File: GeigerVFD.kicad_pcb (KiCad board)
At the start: 2 copper layers, 137.2 x 114.3 mm, 68 parts, among them IC1 TLC555, IC2 LM555, J1 5V, J2 3.3V, J3 GND, J4 Pulse, Q1 BD137, T1 STN0214, T2 2N4401, T3 2N4401, T4 Transformer_1P_SS, U1 LM2577, U2 ESP32-DEVKITC-32D, U3 MAX6934, U4 FV651G

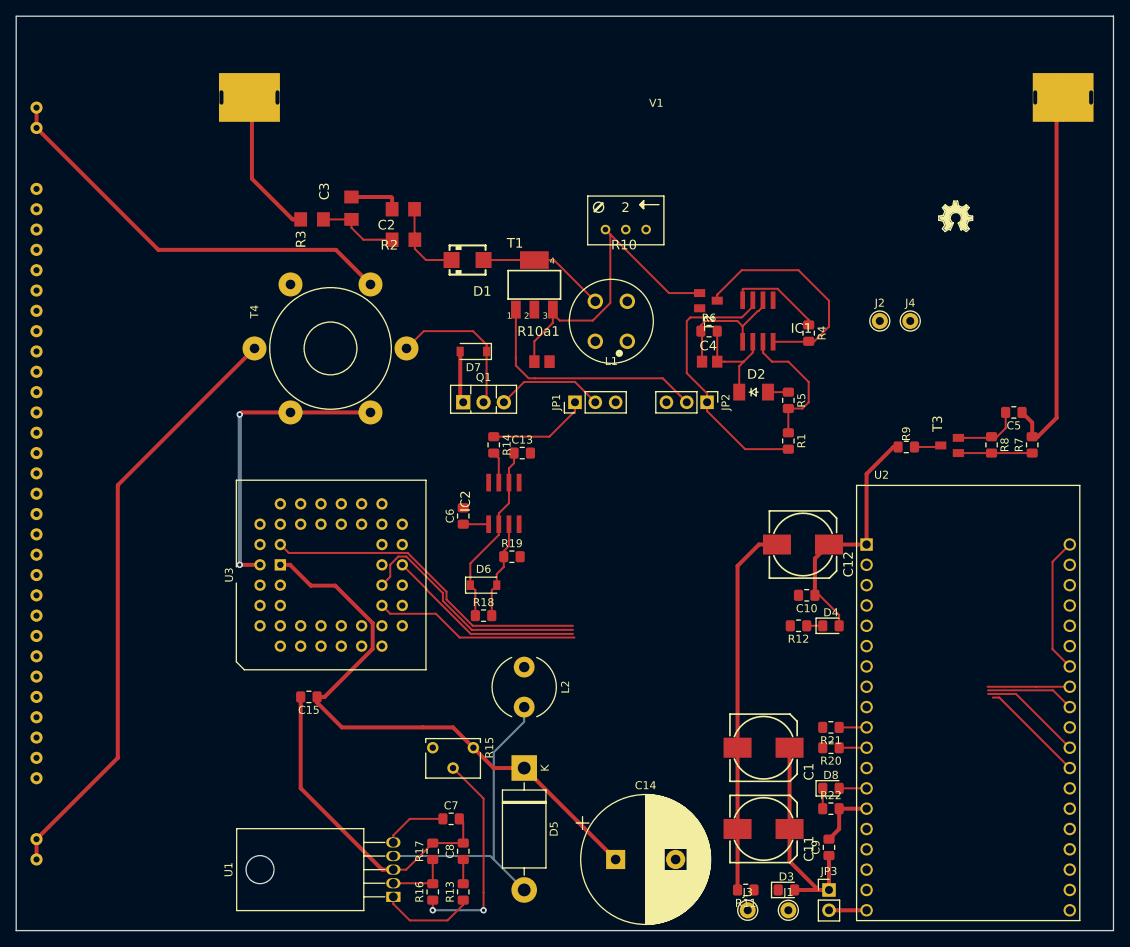
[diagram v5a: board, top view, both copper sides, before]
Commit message: Shrink & route & add rotary encoder & add 3d models
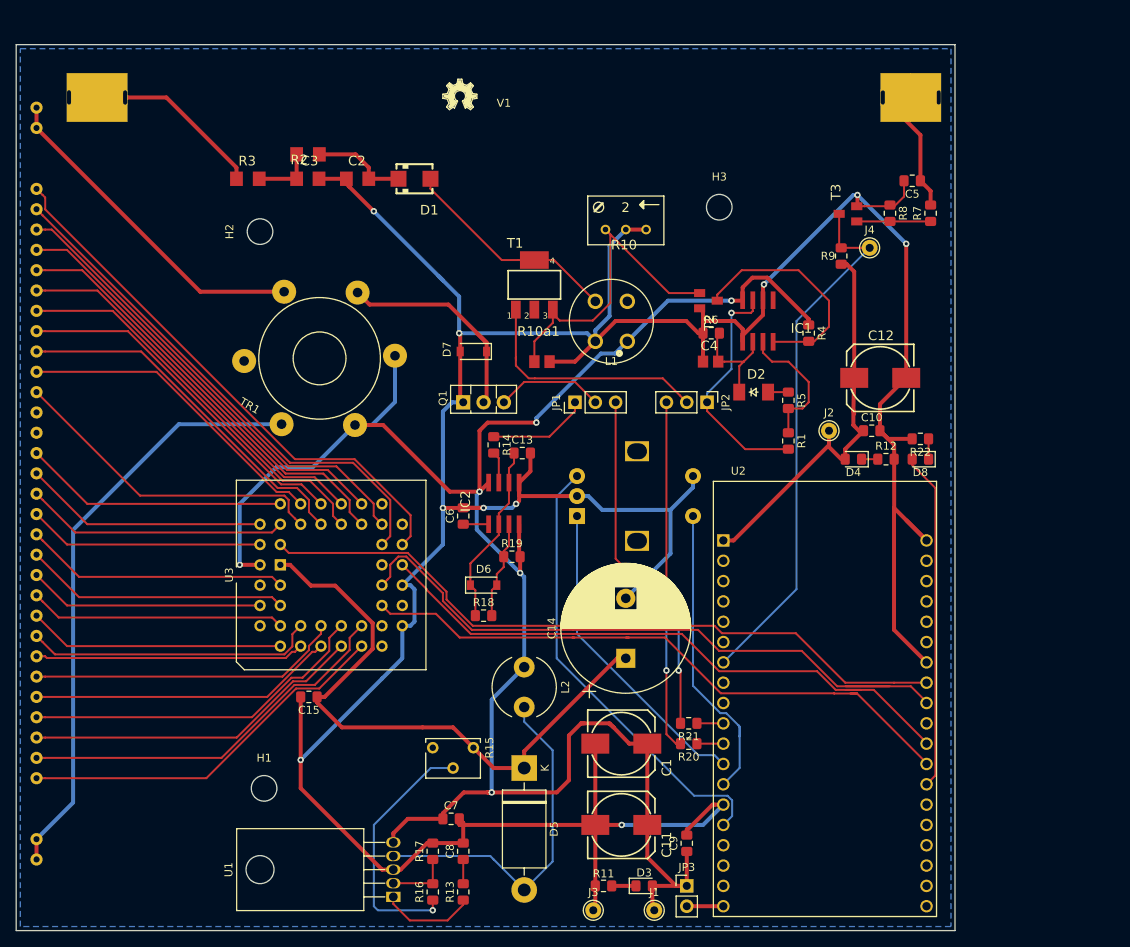
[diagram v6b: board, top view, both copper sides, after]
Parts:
- added H1: MountingHole, MountingHole:MountingHole_3.2mm_M3_DIN965, F.Cu at (29.5, 302.8)
- added H2: MountingHole, MountingHole:MountingHole_3.2mm_M3_DIN965, F.Cu at (29.0, 233.2)
- added H3: MountingHole, MountingHole:MountingHole_3.2mm_M3_DIN965, F.Cu at (86.4, 230.1)
- added SW1: Rotary_Encoder_Switch, Rotary_Encoder:RotaryEncoder_Alps_EC12E-Switch_Vertical_H20mm, B.Cu at (68.6, 268.7)
- moved LOGO1 63.8 mm to (51.8, 217.9)
- moved R22 47.6 mm to (111.5, 259.1), turned to 180 degrees
- moved D8 42.6 mm to (111.5, 261.6), turned to 180 degrees
- moved R7 31.6 mm to (112.8, 230.9)
- moved R8 31.6 mm to (107.7, 230.9)
- moved T3 31.6 mm to (102.4, 231.0)
- moved C5 31.6 mm to (110.5, 226.8)
- moved R9 25.2 mm to (101.6, 236.2), turned to 90 degrees
- moved C14 25.2 mm to (74.7, 286.5), turned to 90 degrees
- moved R12 23.5 mm to (107.2, 261.6), turned to 0 degrees
- moved C12 23.0 mm to (106.5, 251.5), turned to 180 degrees
- moved C10 22.1 mm to (105.4, 258.1), turned to 0 degrees
- moved D4 21.0 mm to (103.1, 261.6), turned to 180 degrees
- moved J3 19.3 mm to (70.6, 318.0)
- moved V1 19.1 mm to (59.4, 216.4)
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- renumbered T4 to TR1
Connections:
- net Net-(U3-Pad34) renamed /05G
- U2 pad 12: (no net) -> Net-(SW1-PadA)
- U2 pad 13: Net-(D8-Pad2) -> Net-(SW1-PadS1)
- U2 pad 15: (no net) -> Net-(SW1-PadB)
- U2 pad 32: (no net) -> Net-(D8-Pad2)
- U3 pad 10: Net-(U3-Pad10) -> /P10
- U3 pad 11: Net-(U3-Pad11) -> /P13
- U3 pad 12: Net-(U3-Pad12) -> /P12
- U3 pad 13: Net-(U3-Pad13) -> /P15
- U3 pad 14: Net-(U3-Pad14) -> /P14
- U3 pad 15: Net-(U3-Pad15) -> /P17
- U3 pad 16: Net-(U3-Pad16) -> /P16
- U3 pad 17: Net-(U3-Pad17) -> (no net)
- U3 pad 19: Net-(U3-Pad19) -> (no net)
- U3 pad 20: Net-(U3-Pad20) -> (no net)
- U3 pad 25: Net-(U3-Pad25) -> (no net)
- U3 pad 26: (no net) -> /11G
- U3 pad 27: (no net) -> /10G
- U3 pad 3: Net-(U3-Pad3) -> /P05
- U3 pad 30: Net-(U3-Pad30) -> /09G
- U3 pad 31: Net-(U3-Pad31) -> /08G
- U3 pad 32: Net-(U3-Pad32) -> /07G
- U3 pad 33: Net-(U3-Pad33) -> /06G
- U3 pad 35: Net-(U3-Pad35) -> /04G
- U3 pad 36: Net-(U3-Pad36) -> /03G
- U3 pad 37: Net-(U3-Pad37) -> /02G
- U3 pad 38: Net-(U3-Pad38) -> /01G
- U3 pad 39: Net-(U3-Pad39) -> /P01
- U3 pad 4: Net-(U3-Pad4) -> /P07
- U3 pad 40: Net-(U3-Pad40) -> /P02
- U3 pad 41: (no net) -> /P03
- U3 pad 42: (no net) -> /P04
- U3 pad 5: Net-(U3-Pad5) -> /P06
- U3 pad 7: Net-(U3-Pad7) -> /P09
- U3 pad 8: Net-(U3-Pad8) -> /P08
- U3 pad 9: Net-(U3-Pad9) -> /P11
- U4 pad 10: Net-(U3-Pad9) -> /P12
- U4 pad 11: Net-(U3-Pad10) -> /P11
- U4 pad 12: Net-(U3-Pad11) -> /P10
- U4 pad 13: Net-(U3-Pad12) -> /P09
- U4 pad 14: Net-(U3-Pad13) -> /P08
- U4 pad 15: Net-(U3-Pad14) -> /P07
- U4 pad 16: Net-(U3-Pad15) -> /P06
- U4 pad 17: Net-(U3-Pad16) -> /P05
- U4 pad 18: Net-(U3-Pad17) -> /P04
- U4 pad 19: Net-(U3-Pad19) -> /P03
- U4 pad 20: Net-(U3-Pad20) -> /P02
- U4 pad 21: Net-(U3-Pad25) -> /P01
- U4 pad 24: Net-(U3-Pad30) -> /01G
- U4 pad 25: Net-(U3-Pad31) -> /02G
- U4 pad 26: Net-(U3-Pad32) -> /03G
- U4 pad 27: Net-(U3-Pad33) -> /04G
- U4 pad 29: Net-(U3-Pad35) -> /06G
- U4 pad 30: Net-(U3-Pad36) -> /07G
- U4 pad 31: Net-(U3-Pad37) -> /08G
- U4 pad 32: Net-(U3-Pad38) -> /09G
- U4 pad 33: Net-(U3-Pad39) -> /10G
- U4 pad 34: Net-(U3-Pad40) -> /11G
- U4 pad 5: Net-(U3-Pad3) -> /P17
- U4 pad 6: Net-(U3-Pad4) -> /P16
- U4 pad 7: Net-(U3-Pad5) -> /P15
- U4 pad 8: Net-(U3-Pad7) -> /P14
- U4 pad 9: Net-(U3-Pad8) -> /P13
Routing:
- net GND: track 150.1 -> 444.8 mm, vias 0 -> 10
- net +5V: track 86.8 -> 247.4 mm, vias 2 -> 6
- net /11G: track 0.00 -> 68.6 mm
- net /10G: track 0.00 -> 65.3 mm
- net Net-(J4-Pad1): track 3.36 -> 67.3 mm
- net /09G: track 0.00 -> 59.3 mm
- net Net-(SW1-PadB): track 0.00 -> 56.6 mm
- net /07G: track 0.00 -> 54.7 mm
- net /08G: track 0.00 -> 53.8 mm
- net /05G: track 0.00 -> 50.0 mm
- net /06G: track 0.00 -> 49.1 mm
- net /P16: track 0.00 -> 48.4 mm
- net /P17: track 0.00 -> 47.5 mm
- net Net-(JP1-Pad3): track 0.00 -> 47.3 mm, vias 0 -> 2
- net /03G: track 0.00 -> 45.4 mm
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- added copper zone on B.Cu, net GND
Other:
- board size 137.2 x 114.3 mm -> 117.3 x 110.7 mm

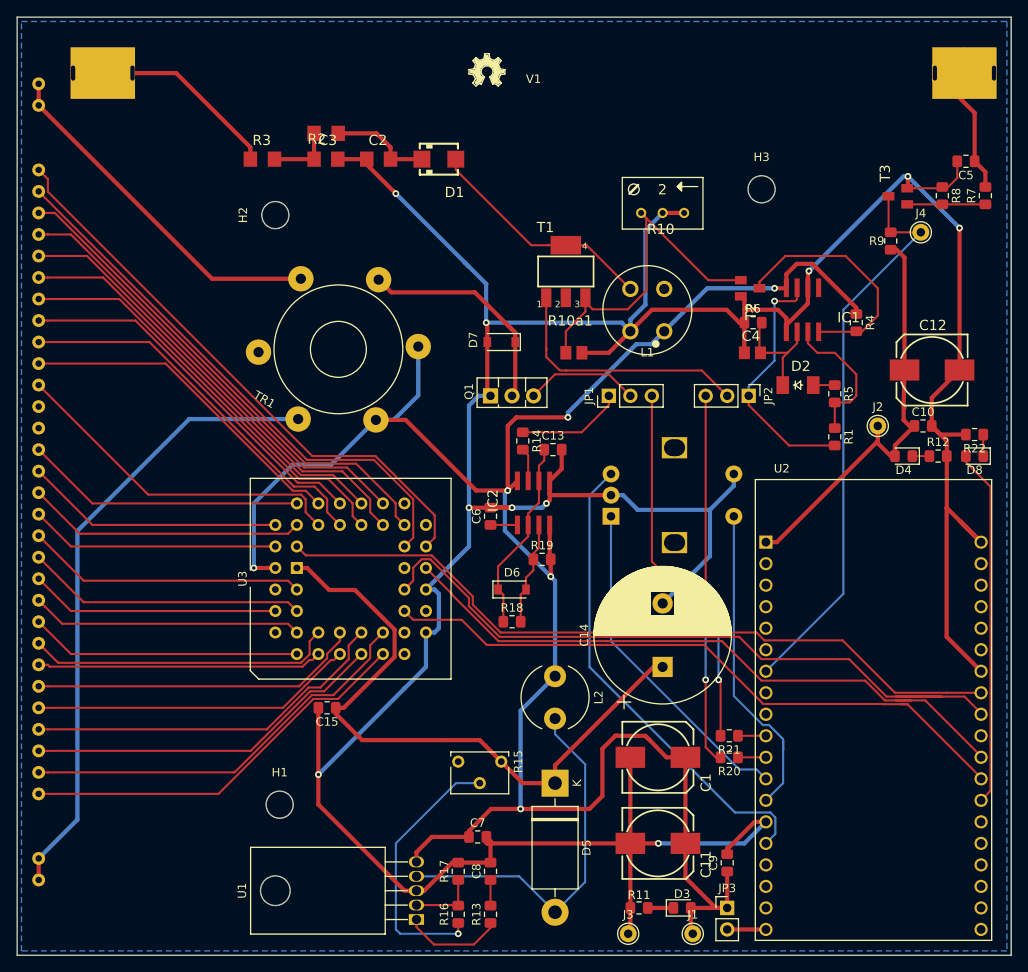
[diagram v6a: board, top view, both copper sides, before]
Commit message: Convert Eagle R to Kicad Add Buzzer header & Warn LED
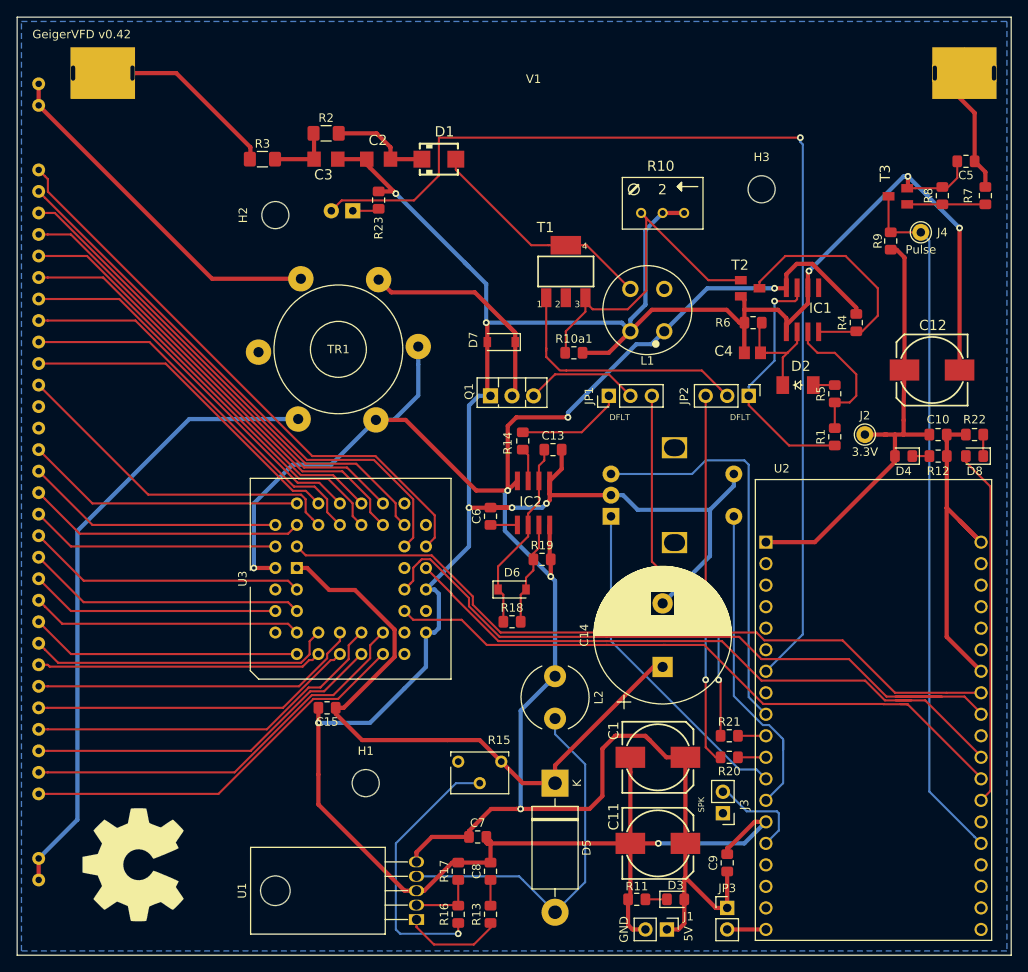
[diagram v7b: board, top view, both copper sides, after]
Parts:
- added D9: red, LED_THT:LED_D5.0mm, B.Cu at (38.1, 232.7)
- added R23: 1k, Resistor_SMD:R_0805_2012Metric_Pad1.15x1.40mm_HandSolder, F.Cu at (41.1, 231.4)
- J1: value 5V -> Conn_01x02_Male; footprint Connector_Pin:Pin_D1.0mm_L10.0mm -> Connector_PinHeader_2.54mm:PinHeader_1x02_P2.54mm_Vertical
- J3: value GND -> Conn_01x02_Male; footprint Connector_Pin:Pin_D1.0mm_L10.0mm -> Connector_PinHeader_2.54mm:PinHeader_1x02_P2.54mm_Vertical
- LOGO1: value OSHW_LOGO_FILLX0150-NT -> Logo_Open_Hardware_Large; footprint PiGI-V1.1:OSHW_FILLX150_NOTEXT -> Symbol:OSHW-Symbol_13.4x12mm_SilkScreen
- R10a1: footprint PiGI-V1.1:M0805 -> Resistor_SMD:R_0805_2012Metric_Pad1.15x1.40mm_HandSolder
- R2, R3: footprint PiGI-V1.1:R1206 -> Resistor_SMD:R_1206_3216Metric_Pad1.42x1.75mm_HandSolder
- moved LOGO1 100.1 mm to (12.2, 309.9), turned to 90 degrees
- moved J3 18.1 mm to (81.8, 303.8)
- moved H1 10.5 mm to (39.6, 300.2)
- moved J1 3.09 mm to (75.2, 317.5), turned to 270 degrees
- moved C10 2.04 mm to (107.2, 259.1)
- moved J2 1.83 mm to (98.6, 259.1)
- moved D3 1.27 mm to (76.2, 313.9)
- moved R11 1.05 mm to (71.6, 313.9)
- turned R1 to 90 degrees
- turned R10a1 to 0 degrees
- turned R2 to 0 degrees
- turned R21 to 0 degrees
- turned R3 to 0 degrees
- turned R4 to 90 degrees
- turned R5 to 90 degrees
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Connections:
- C5 pad 1: HV- -> /HV-
- R1 pad 1: Net-(IC1-Pad3) -> Net-(IC1-Pad7)
- R1 pad 2: Net-(IC1-Pad7) -> Net-(IC1-Pad3)
- R10a1 pad 1: GND -> Net-(R10-PadA)
- R10a1 pad 2: Net-(R10-PadA) -> GND
- R2 pad 1: Net-(C2-Pad1) -> Net-(C3-Pad1)
- R2 pad 2: Net-(C3-Pad1) -> Net-(C2-Pad1)
- R21 pad 1: Net-(R21-Pad1) -> Net-(JP2-Pad3)
- R21 pad 2: Net-(JP2-Pad3) -> Net-(R21-Pad2)
- R3 pad 1: Net-(C3-Pad1) -> /HV+
- R3 pad 2: HV+ -> Net-(C3-Pad1)
- R4 pad 1: +5V -> R
- R4 pad 2: R -> +5V
- R5 pad 1: Net-(D2-PadA) -> Net-(IC1-Pad3)
- R5 pad 2: Net-(IC1-Pad3) -> Net-(D2-PadA)
- R6 pad 1: GND -> Net-(C4-Pad2)
- R6 pad 2: Net-(C4-Pad2) -> GND
- R7 pad 1: Net-(R7-Pad1) -> /HV-
- R7 pad 2: HV- -> Net-(R7-Pad2)
- R8 pad 1: GND -> Net-(R7-Pad2)
- R8 pad 2: Net-(R7-Pad1) -> GND
- R9 pad 1: +3V3 -> Net-(J4-Pad1)
- R9 pad 2: Net-(J4-Pad1) -> +3V3
- T3 pad 1: Net-(R7-Pad1) -> Net-(R7-Pad2)
- U2 pad 10: Net-(R21-Pad1) -> Net-(R21-Pad2)
- U2 pad 15: Net-(SW1-PadB) -> Net-(J3-Pad2)
- U2 pad 34: (no net) -> Net-(J4-Pad1)
- U2 pad 7: Net-(J4-Pad1) -> Net-(D9-Pad2)
- U2 pad 9: (no net) -> Net-(SW1-PadB)
- V1 pad 1: HV+ -> /HV+
- V1 pad 2: HV- -> /HV-
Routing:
- net Net-(D9-Pad2): track 0.00 -> 126.5 mm, vias 0 -> 1
- net HV+: track 26.0 -> 0.00 mm
- net /HV+: track 0.00 -> 26.0 mm
- net HV-: track 22.9 -> 0.00 mm
- net /HV-: track 0.00 -> 22.9 mm
- net Net-(J4-Pad1): track 67.3 -> 83.0 mm
- net Net-(J3-Pad2): track 0.00 -> 12.1 mm
- net GND: track 444.8 -> 433.8 mm
- net Net-(R7-Pad2): track 0.00 -> 9.23 mm
- net Net-(R7-Pad1): track 9.23 -> 0.00 mm
- net Net-(SW1-PadB): track 56.6 -> 47.4 mm
- net Net-(R21-Pad1): track 3.43 -> 0.00 mm
- net Net-(R21-Pad2): track 0.00 -> 3.30 mm
- net Net-(D9-Pad1): track 0.00 -> 3.15 mm
- net +3V3: track 50.3 -> 53.2 mm
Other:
- board text added: "GeigerVFD v0.42"

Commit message: Finish PCB
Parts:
- moved D9 13.7 mm to (51.8, 233.0), turned to 0 degrees
- moved H2 10.5 mm to (39.5, 233.0)
- moved R23 5.59 mm to (46.7, 231.6)
- moved H3 2.88 mm to (86.4, 233.0)
- moved H1 0.12 mm to (39.5, 300.2)
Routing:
- net Net-(D9-Pad2): track 126.5 -> 121.5 mm
- net Net-(D9-Pad1): track 3.15 -> 5.22 mm
- net GND: track 433.8 -> 435.5 mm
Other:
- board size 117.3 x 110.7 mm -> 117.3 x 109.7 mm
- board text added: "2020-05-13"
- board text added: "JLCJLCJLCJLC"
